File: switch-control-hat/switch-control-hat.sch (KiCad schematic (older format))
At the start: 42 parts, among them J1 Conn_01x09, J2 Frontend Connector, J3 Conn_01x02, J4 Power Connector, P1 RPi-Header, SW1 SW_Push, U1 TLP3543, U2 TLP3543, U3 TLP3543, U4 TLP3543, U5 TLP3543, U6 TLP3543, U7 TLP3543, U8 TLP3543, U9 DS3231M

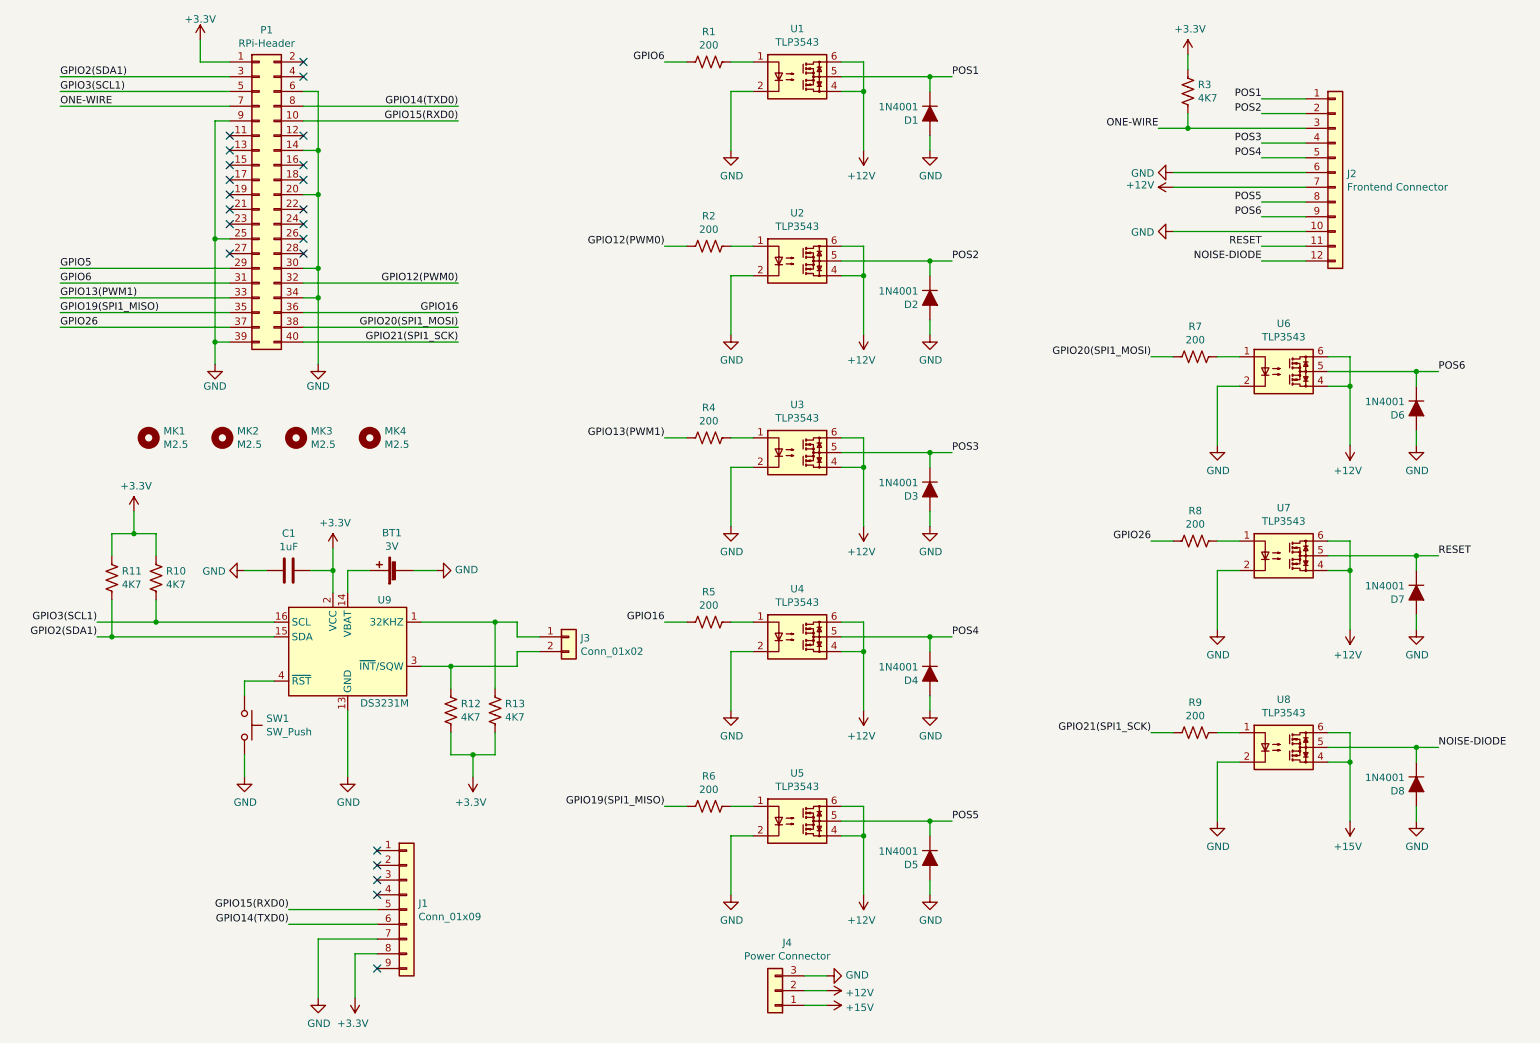
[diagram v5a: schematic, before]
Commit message: Updated to control second frontend switch
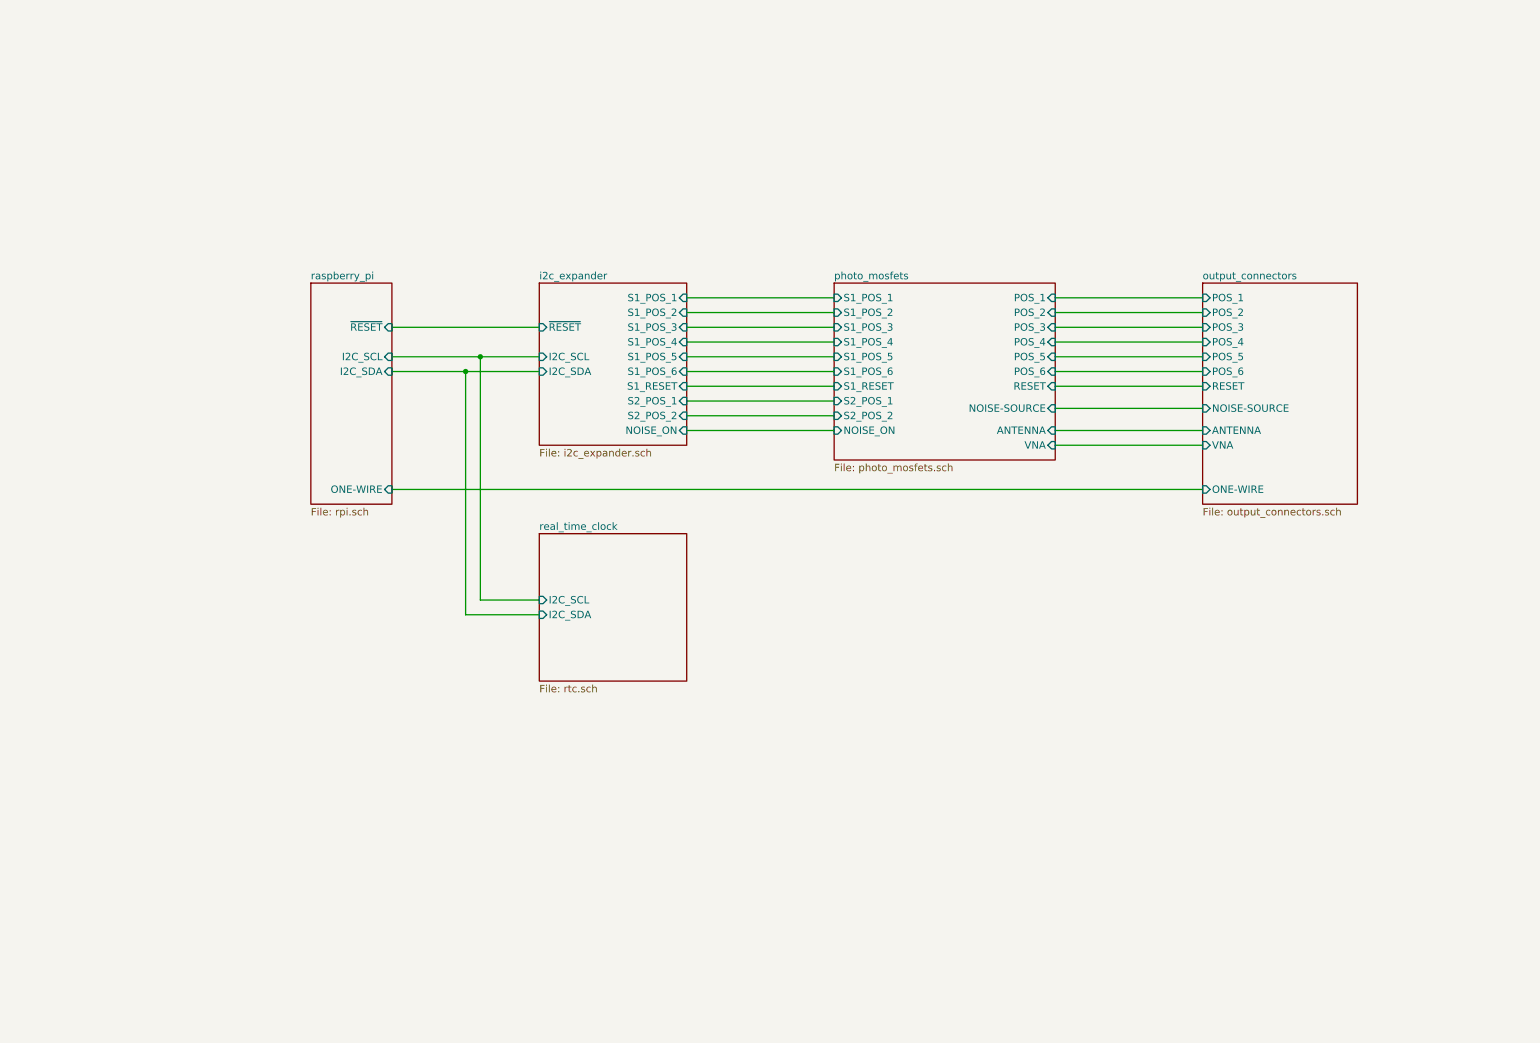
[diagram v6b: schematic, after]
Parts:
- removed BT1: 3V, Battery:BatteryHolder_Keystone_3000_1x12mm, symbol Device:Battery_Cell
- removed C1: 1uF, Capacitor_SMD:C_0603_1608Metric_Pad1.05x0.95mm_HandSolder, symbol Device:C
- removed D1, D2, D3, D4, D5, D6, D7, D8: 1N4001, Diode_THT:D_DO-41_SOD81_P3.81mm_Vertical_AnodeUp, symbol Device:D_ALT
- removed J1: Conn_01x09, Connector_PinSocket_2.54mm:PinSocket_1x09_P2.54mm_Vertical, symbol Connector_Generic:Conn_01x09
- removed J2: Frontend Connector, Connector_Phoenix_MC:PhoenixContact_MC_1,5_12-G-3.81_1x12_P3.81mm_Horizontal, symbol Connector_Generic:Conn_01x12
- removed J3: Conn_01x02, Connector_PinHeader_2.54mm:PinHeader_1x02_P2.54mm_Vertical, symbol Connector_Generic:Conn_01x02
- removed J4: Power Connector, Connector_Phoenix_MC:PhoenixContact_MC_1,5_3-G-3.81_1x03_P3.81mm_Horizontal, symbol Connector_Generic:Conn_01x03
- removed MK1, MK2, MK3, MK4: M2.5, MountingHole:MountingHole_2.7mm_M2.5, symbol switch-control-hat-rescue:Mounting_Hole-Mechanical
- removed P1: RPi-Header, Connector_PinSocket_2.54mm:PinSocket_2x20_P2.54mm_Vertical, symbol Connector_Generic:Conn_02x20_Odd_Even
- removed R1, R2, R4, R5, R6, R7, R8, R9: 200, Resistor_SMD:R_0603_1608Metric_Pad1.05x0.95mm_HandSolder, symbol Device:R_US
- removed R10, R11, R12, R13, R3: 4K7, Resistor_SMD:R_0603_1608Metric_Pad1.05x0.95mm_HandSolder, symbol Device:R_US
- removed SW1: SW_Push, Button_Switch_SMD:SW_Push_SPST_NO_Alps_SKRK, symbol Switch:SW_Push
- removed U1, U2, U3, U4, U5, U6, U7, U8: TLP3543, Package_DIP:DIP-6_W7.62mm, symbol Relay_SolidState:TLP3543
- removed U9: DS3231M, Package_SO:SOIC-16W_7.5x10.3mm_P1.27mm, symbol Timer_RTC:DS3231M
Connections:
- no-connect marks 22 -> 0
